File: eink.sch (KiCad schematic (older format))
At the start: 10 parts, among them P5 eInk

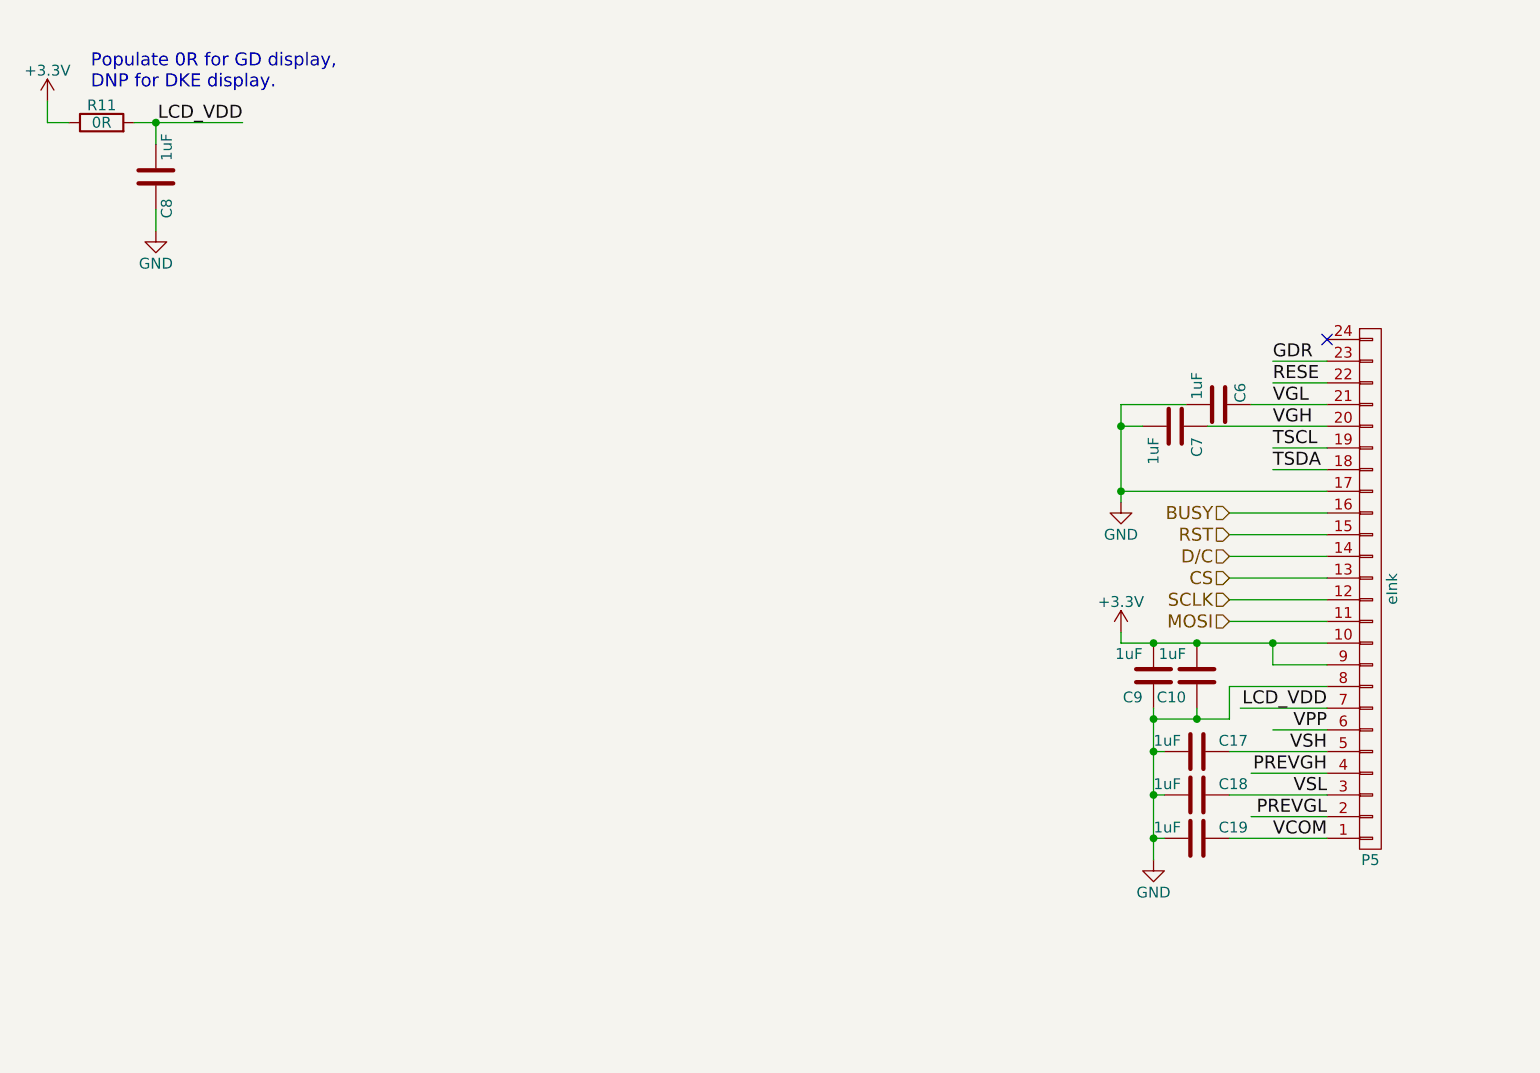
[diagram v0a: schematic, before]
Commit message: Add e-ink gate drive circuitry
Closes #14
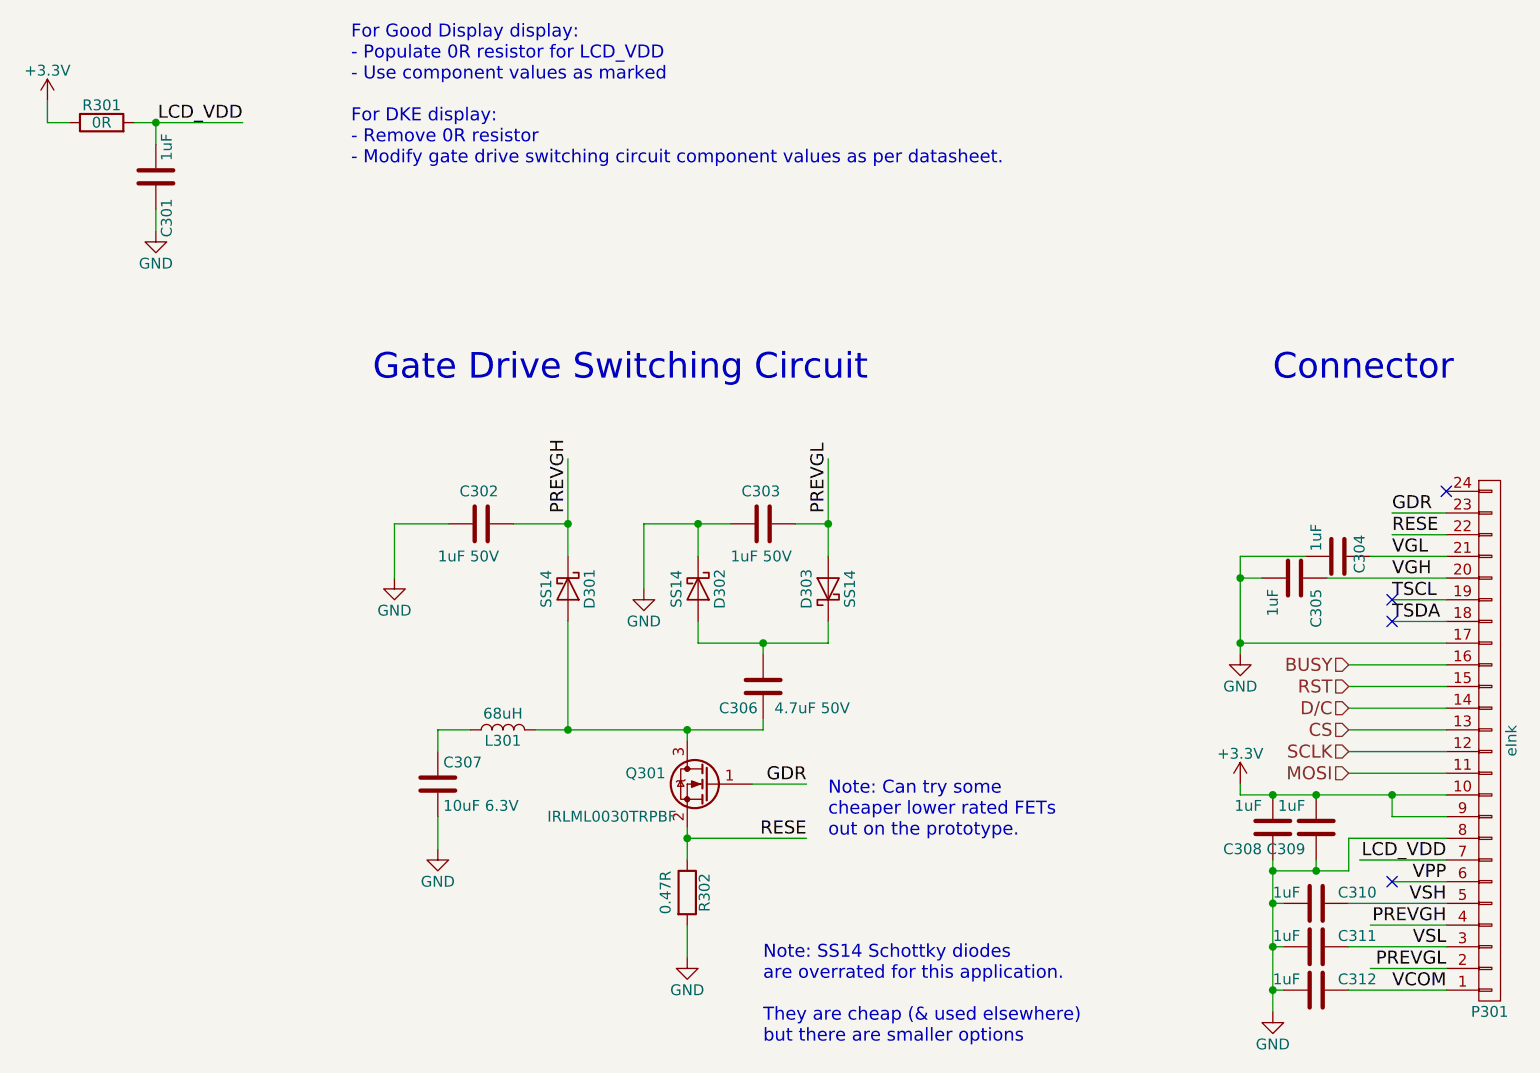
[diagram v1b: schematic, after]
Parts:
- added C302, C303: 1uF 50V, symbol C
- added C306: 4.7uF 50V, symbol C
- added C307: 10uF 6.3V, symbol C
- added D301, D302, D303: SS14, symbol D_Schottky
- added L301: 68uH, symbol L
- added Q301: IRLML0030TRPBF, TO_SOT_Packages_SMD:SOT-23, symbol Q_NMOS_GSD
- added R302: 0.47R, symbol R
- renumbered C8 to C301, C6 to C304, C7 to C305, C9 to C308, C10 to C309, C17 to C310, C18 to C311, C19 to C312, P5 to P301, R11 to R301
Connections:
- wire segments 40 -> 64
- no-connect marks 1 -> 4
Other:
- note added: "Connector"
- note added: "For Good Display display:\n- Populate 0R resistor for LCD_VDD\n- Use component values as marked\n\nFor DKE display:\n- Remove 0R resistor\n- Modify gate drive switching circuit component values as per datasheet."
- note added: "Gate Drive Switching Circuit"
- note added: "Note: Can try some\ncheaper lower rated FETs\nout on the prototype."
- note added: "Note: SS14 Schottky diodes\nare overrated for this application.\n\nThey are cheap (& used elsewhere)\nbut there are smaller options"
- note removed: "Populate 0R for GD display, \nDNP for DKE display."
- moved on the sheet: C304, C305, C308, C309, C310, C311, C312, P301

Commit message: Set component footprints.
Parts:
- C302, C303, C306: footprint (none) -> Capacitors_SMD:C_0603_HandSoldering
- C307: footprint (none) -> Capacitors_SMD:C_0805_HandSoldering
- D301, D302, D303: footprint (none) -> Diodes_SMD:D_SMA
- R302: footprint (none) -> Resistors_SMD:R_0603_HandSoldering
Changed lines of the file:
@@
 F 0 "C307" H 3075 4300 50  0000 L CNN
 F 1 "10uF 6.3V" H 3075 4100 50  0000 L CNN
-F 2 "" H 3088 4050 50  0001 C CNN
+F 2 "Capacitors_SMD:C_0805_HandSoldering" H 3088 4050 50  0001 C CNN
 F 3 "" H 3050 4200 50  0001 C CNN
 	1    3050 4200
@@
 F 0 "D301" H 3650 3400 50  0000 C CNN
 F 1 "SS14" H 3650 3200 50  0000 C CNN
-F 2 "" H 3650 3300 50  0001 C CNN
+F 2 "Diodes_SMD:D_SMA" H 3650 3300 50  0001 C CNN
 F 3 "" H 3650 3300 50  0001 C CNN
 	1    3650 3300
@@
 F 0 "C302" V 3100 2900 50  0000 L CNN
 F 1 "1uF 50V" V 3400 2800 50  0000 L CNN
-F 2 "" H 3288 2850 50  0001 C CNN
+F 2 "Capacitors_SMD:C_0603_HandSoldering" H 3288 2850 50  0001 C CNN
 F 3 "" H 3250 3000 50  0001 C CNN
 	1    3250 3000
@@
 F 0 "D302" H 4250 3400 50  0000 C CNN
 F 1 "SS14" H 4250 3200 50  0000 C CNN
-F 2 "" H 4250 3300 50  0001 C CNN
+F 2 "Diodes_SMD:D_SMA" H 4250 3300 50  0001 C CNN
 F 3 "" H 4250 3300 50  0001 C CNN
 	1    4250 3300
@@
 F 0 "C303" V 4400 2900 50  0000 L CNN
 F 1 "1uF 50V" V 4700 2850 50  0000 L CNN
-F 2 "" H 4588 2850 50  0001 C CNN
+F 2 "Capacitors_SMD:C_0603_HandSoldering" H 4588 2850 50  0001 C CNN
 F 3 "" H 4550 3000 50  0001 C CNN
 	1    4550 3000
@@
 F 0 "D303" H 4850 3400 50  0000 C CNN
 F 1 "SS14" H 4850 3200 50  0000 C CNN
-F 2 "" H 4850 3300 50  0001 C CNN
+F 2 "Diodes_SMD:D_SMA" H 4850 3300 50  0001 C CNN
 F 3 "" H 4850 3300 50  0001 C CNN
 	1    4850 3300
@@
 F 0 "C306" H 4575 3850 50  0000 L CNN
 F 1 "4.7uF 50V" H 4150 3850 50  0000 L CNN
-F 2 "" H 4588 3600 50  0001 C CNN
+F 2 "Capacitors_SMD:C_0603_HandSoldering" H 4588 3600 50  0001 C CNN
 F 3 "" H 4550 3750 50  0001 C CNN
 	1    4550 3750
@@
 F 0 "R302" V 4280 4700 50  0000 C CNN
 F 1 "0.47R" V 4100 4700 50  0000 C CNN
-F 2 "" V 4130 4700 50  0001 C CNN
+F 2 "Resistors_SMD:R_0603_HandSoldering" V 4130 4700 50  0001 C CNN
 F 3 "" H 4200 4700 50  0001 C CNN
 	1    4200 4700

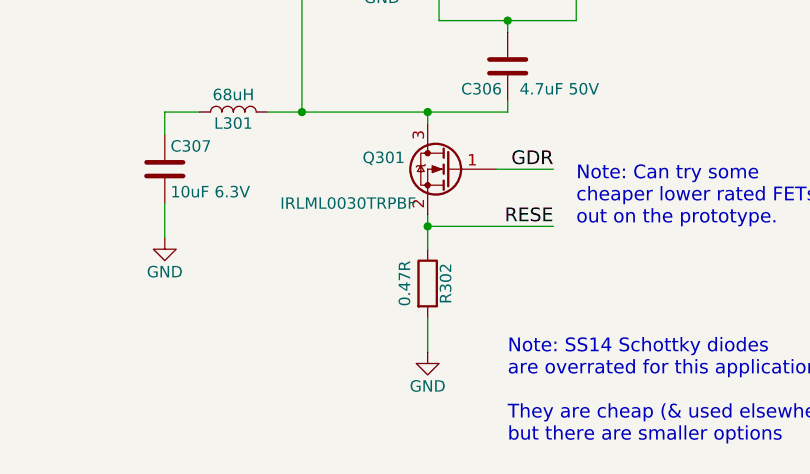
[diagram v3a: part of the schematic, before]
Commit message: Minor updates to schematic components.
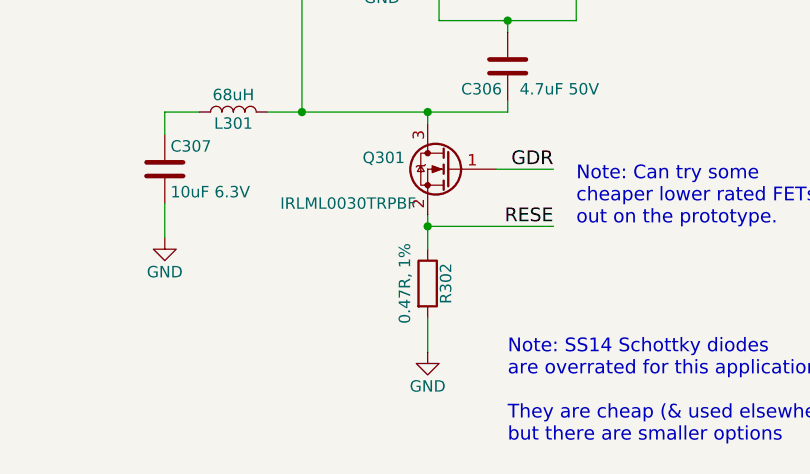
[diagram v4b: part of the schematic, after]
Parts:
- R302: value 0.47R -> 0.47R, 1%
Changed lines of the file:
@@
 P 4200 4700
 F 0 "R302" V 4280 4700 50  0000 C CNN
-F 1 "0.47R" V 4100 4700 50  0000 C CNN
+F 1 "0.47R, 1%" V 4100 4700 50  0000 C CNN
 F 2 "Resistors_SMD:R_0603_HandSoldering" V 4130 4700 50  0001 C CNN
 F 3 "" H 4200 4700 50  0001 C CNN

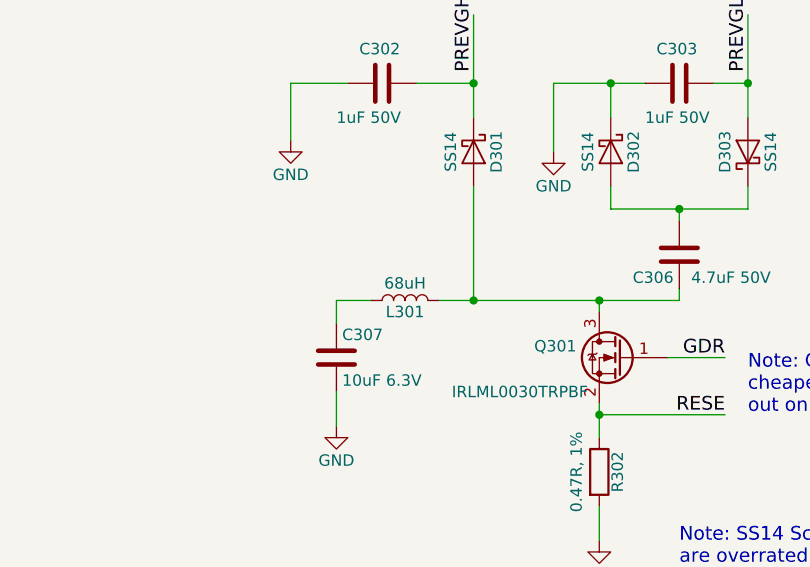
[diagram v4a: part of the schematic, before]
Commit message: Picked inductor.
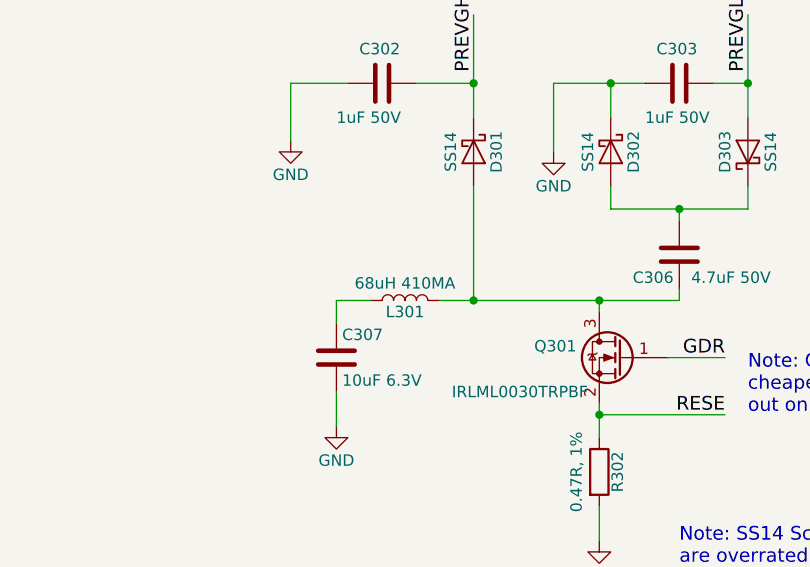
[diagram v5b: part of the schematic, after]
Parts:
- L301: value 68uH -> 68uH 410MA; footprint (none) -> Capacitors_SMD:C_1210_HandSoldering; Description (none) -> FIXED IND 68UH 410MA 1.3 OHM 1210 SMD; Digikey PN (none) -> 587-3070-1-ND; MPN (none) -> CBC3225T680KR
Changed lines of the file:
@@
 P 3350 3950
 F 0 "L301" V 3300 3950 50  0000 C CNN
-F 1 "68uH" V 3425 3950 50  0000 C CNN
-F 2 "" H 3350 3950 50  0001 C CNN
+F 1 "68uH 410MA" V 3425 3950 50  0000 C CNN
+F 2 "Capacitors_SMD:C_1210_HandSoldering" H 3350 3950 50  0001 C CNN
 F 3 "" H 3350 3950 50  0001 C CNN
+F 4 "CBC3225T680KR" V 3350 3950 60  0001 C CNN "MPN"
+F 5 "587-3070-1-ND" V 3350 3950 60  0001 C CNN "Digikey PN"
+F 6 "FIXED IND 68UH 410MA 1.3 OHM 1210 SMD" V 3350 3950 60  0001 C CNN "Description"
 	1    3350 3950
 	0    -1   -1   0

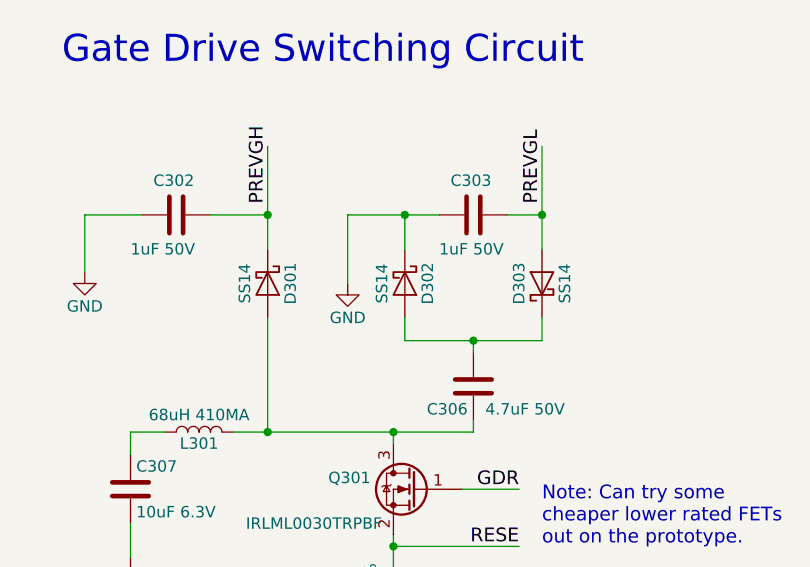
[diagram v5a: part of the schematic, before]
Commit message: Changed drive circuitry Schottky diodes to SOD323.
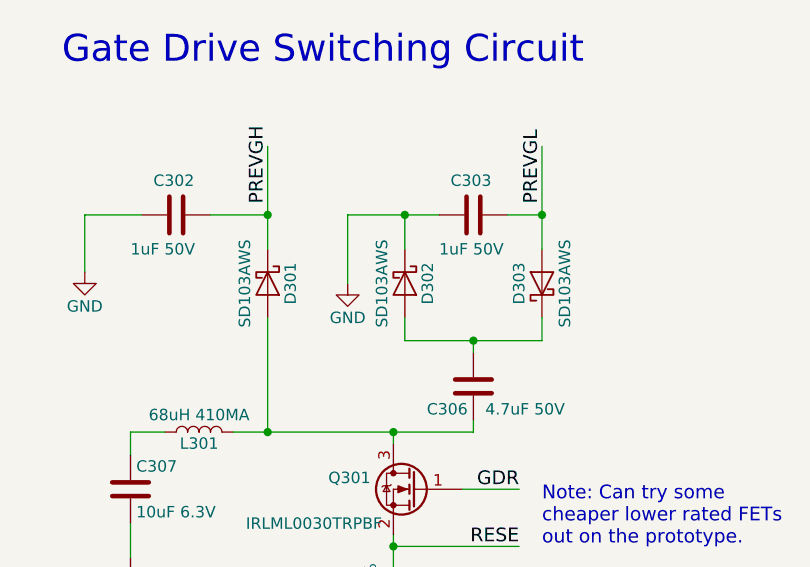
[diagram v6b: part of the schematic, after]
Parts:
- D301, D302, D303: value SS14 -> SD103AWS; footprint Diodes_SMD:D_SMA -> Diodes_SMD:D_SOD-323
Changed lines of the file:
@@
 P 3650 3300
 F 0 "D301" H 3650 3400 50  0000 C CNN
-F 1 "SS14" H 3650 3200 50  0000 C CNN
-F 2 "Diodes_SMD:D_SMA" H 3650 3300 50  0001 C CNN
+F 1 "SD103AWS" H 3650 3200 50  0000 C CNN
+F 2 "Diodes_SMD:D_SOD-323" H 3650 3300 50  0001 C CNN
 F 3 "" H 3650 3300 50  0001 C CNN
 	1    3650 3300
@@
 P 4250 3300
 F 0 "D302" H 4250 3400 50  0000 C CNN
-F 1 "SS14" H 4250 3200 50  0000 C CNN
-F 2 "Diodes_SMD:D_SMA" H 4250 3300 50  0001 C CNN
+F 1 "SD103AWS" H 4250 3200 50  0000 C CNN
+F 2 "Diodes_SMD:D_SOD-323" H 4250 3300 50  0001 C CNN
 F 3 "" H 4250 3300 50  0001 C CNN
 	1    4250 3300
@@
 P 4850 3300
 F 0 "D303" H 4850 3400 50  0000 C CNN
-F 1 "SS14" H 4850 3200 50  0000 C CNN
-F 2 "Diodes_SMD:D_SMA" H 4850 3300 50  0001 C CNN
+F 1 "SD103AWS" H 4850 3200 50  0000 C CNN
+F 2 "Diodes_SMD:D_SOD-323" H 4850 3300 50  0001 C CNN
 F 3 "" H 4850 3300 50  0001 C CNN
 	1    4850 3300
